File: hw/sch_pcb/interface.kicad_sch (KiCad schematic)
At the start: 19 parts, among them J6 HEADER_2x15, U12 SN74LVC2T45DCU, U13 SN74LVC2T45DCU, U14 SN74LVC2T45DCU, U6 AT24CS64-SSHM

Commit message: Update silkscreen and title blocks.
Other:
- title: AIRDOS04A base board -> USTSIPIN03A

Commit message: FIX USTIDs.
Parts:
- R11: UST_ID (none) -> 5c70984612875079b91f899f
- U12, U13, U14: UST_ID (none) -> 65555a850c8d609e3e79abde
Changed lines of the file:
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@@
+      (effects (font (size 1.27 1.27)) hide)
+    )
+    (property "UST_ID" "65555a850c8d609e3e79abde" (at 109.22 99.06 0)
       (effects (font (size 1.27 1.27)) hide)
     )
@@
       (effects (font (size 1.27 1.27)) hide)
     )
+    (property "UST_ID" "65555a850c8d609e3e79abde" (at 66.04 99.06 0)
+      (effects (font (size 1.27 1.27)) hide)
+    )
     (pin "1")
     (pin "2")
@@
       (effects (font (size 1.27 1.27)) hide)
     )
-    (property "UST_ID" "" (at 72.39 157.48 0)
+    (property "UST_ID" "5c70984612875079b91f899f" (at 72.39 157.48 0)
       (effects (font (size 1.27 1.27)) hide)
     )
@@
       (effects (font (size 1.27 1.27)) hide)
     )
-    (property "UST_ID" "" (at 77.47 157.48 0)
+    (property "UST_ID" "5c70984612875079b91f899f" (at 77.47 157.48 0)
       (effects (font (size 1.27 1.27)) hide)
     )
@@
       (effects (font (size 1.27 1.27)) hide)
     )
+    (property "UST_ID" "65555a850c8d609e3e79abde" (at 157.48 99.06 0)
+      (effects (font (size 1.27 1.27)) hide)
+    )

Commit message: Add notes to power consumption.
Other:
- note added: "+1 mA max"
- note added: "16 μA"
- note added: "POWER INPUT 5.5 mA"
- note removed: "POWER INPUT"
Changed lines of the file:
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@@
     (stroke (width 0) (type default))
   )
-  (text "POWER INPUT" (at 213.36 35.56 0)
+  (text "+1 mA max" (at 50.8 151.13 0)
     (effects (font (size 1.524 1.524)) (justify left bottom))
   )
+  (text "16 μA" (at 153.67 68.58 0)
+    (effects (font (size 1.27 1.27)) (justify left bottom))
+  )
+  (text "16 μA" (at 60.96 67.31 0)
+    (effects (font (size 1.524 1.524)) (justify left bottom))
+  )
+  (text "POWER INPUT 5.5 mA " (at 207.01 34.29 0)
+    (effects (font (size 1.524 1.524)) (justify left bottom))
+  )
+  (text "16 μA" (at 105.41 67.31 0)
+    (effects (font (size 1.27 1.27)) (justify left bottom))
+  )
   (label "3v3" (at 106.68 73.66 90) (fields_autoplaced)

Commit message: Flip side of pinheader connector. Resolve #7
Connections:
- net A0: now also J6.9; no longer J6.10
- net A1: now also J6.11; no longer J6.12
- net B0: now also J6.15; no longer J6.16
- net B1: now also J6.13; no longer J6.14
- net C0: now also J6.19; no longer J6.20
- net C1: now also J6.17; no longer J6.18
- net RX: now also J6.12; no longer J6.11
- net SOCKET_MISO: now also J6.18; no longer J6.17
- net SOCKET_MOSI: now also J6.16; no longer J6.15
- net SOCKET_SCLK: now also J6.20; no longer J6.19
- net TX: now also J6.14; no longer J6.13
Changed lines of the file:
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@@
     )
   )
-  (symbol (lib_id "MLAB_HEADER:HEADER_2x15") (at 246.38 68.58 90) (unit 1)
+  (symbol (lib_id "MLAB_HEADER:HEADER_2x15") (at 246.38 68.58 90) (mirror x) (unit 1)
     (in_bom yes) (on_board yes) (dnp no)
-    (property "Reference" "J6" (at 226.06 67.31 90)
+    (property "Reference" "J6" (at 226.06 69.85 90)
       (effects (font (size 1.524 1.524)) (justify left))
     )

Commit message: Swap MISO and MOSI traces. Resolve #4
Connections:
- net MISO: now also U14.6 (2B); no longer U12.7 (1B)
- net MOSI: now also U12.7 (1B); no longer U14.6 (2B)
- net SOCKET_MISO: now also U14.3 (2A); no longer U12.2 (1A)
- net SOCKET_MOSI: now also U12.2 (1A); no longer U14.3 (2A)
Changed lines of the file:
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@@
     (effects (font (size 1.27 1.27)) (justify right bottom))
   )
-  (label "SOCKET_MOSI" (at 146.05 101.6 180) (fields_autoplaced)
+  (label "SOCKET_MOSI" (at 54.61 96.52 180) (fields_autoplaced)
     (effects (font (size 1.524 1.524)) (justify right bottom))
   )
@@
     (effects (font (size 1.27 1.27)) (justify right bottom))
   )
-  (label "SOCKET_MISO" (at 54.61 96.52 180) (fields_autoplaced)
+  (label "SOCKET_MISO" (at 146.05 101.6 180) (fields_autoplaced)
     (effects (font (size 1.524 1.524)) (justify right bottom))
   )
@@
     (effects (font (size 1.524 1.524)) (justify left))
   )
-  (hierarchical_label "MISO" (shape input) (at 77.47 96.52 0) (fields_autoplaced)
+  (hierarchical_label "MISO" (shape input) (at 170.18 101.6 0) (fields_autoplaced)
     (effects (font (size 1.524 1.524)) (justify left))
   )
-  (hierarchical_label "MOSI" (shape output) (at 170.18 101.6 0) (fields_autoplaced)
+  (hierarchical_label "MOSI" (shape output) (at 77.47 96.52 0) (fields_autoplaced)
     (effects (font (size 1.524 1.524)) (justify left))
   )

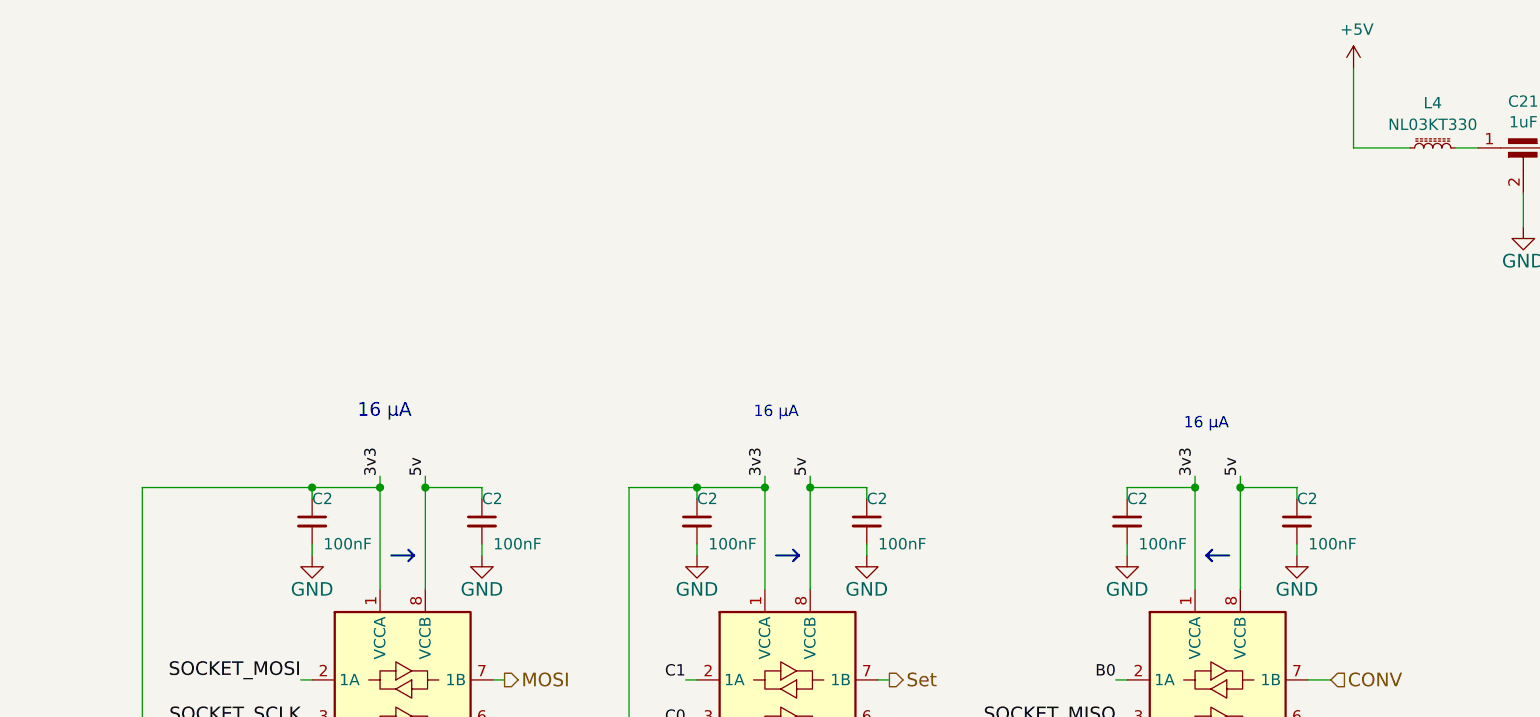
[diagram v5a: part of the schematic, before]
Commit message: Add LDO to power 3.3V translators. Resolve #3
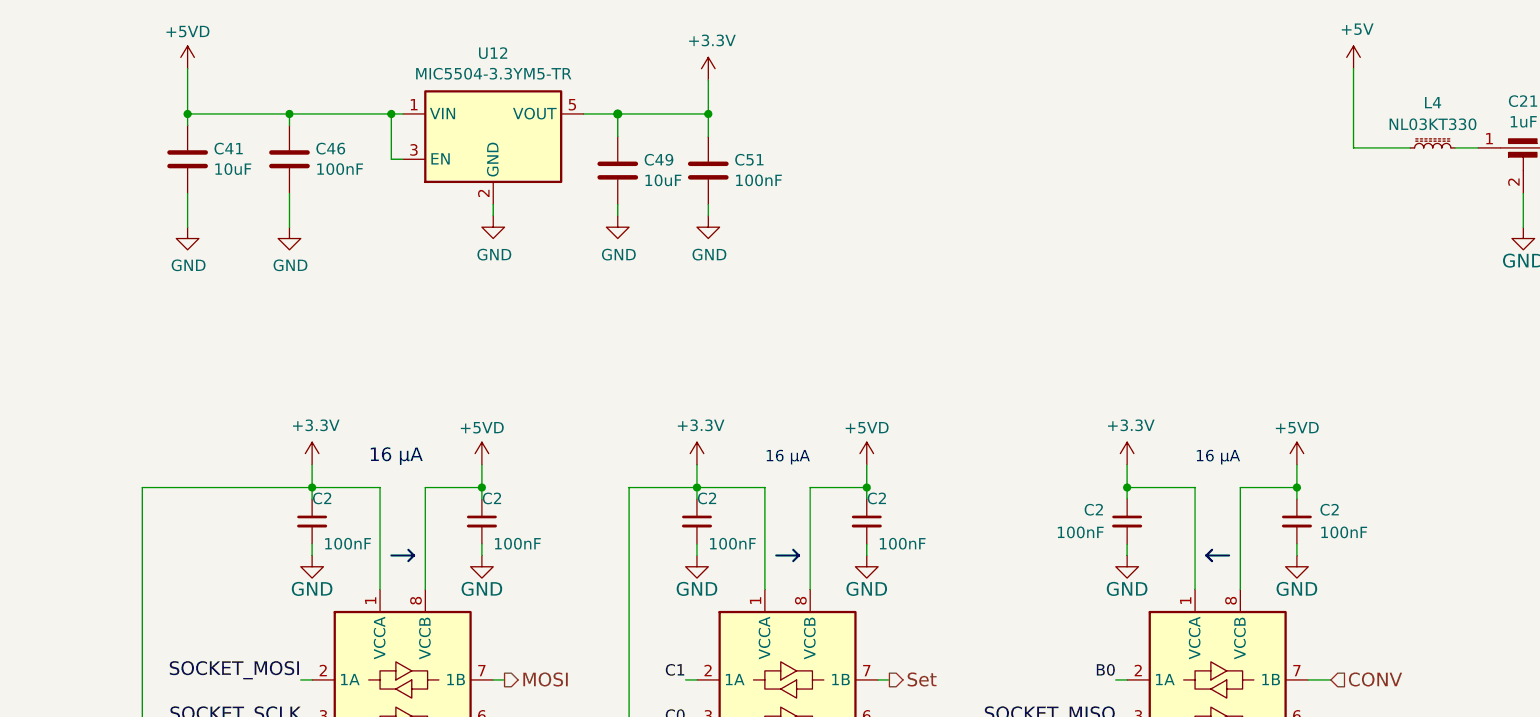
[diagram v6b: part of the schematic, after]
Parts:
- added C41, C49: 10uF, Capacitor_SMD:C_0805_2012Metric, symbol Device:C
- added C46, C51: 100nF, Capacitor_SMD:C_0805_2012Metric, symbol Device:C
- added U12: MIC5504-3.3YM5-TR, Package_TO_SOT_SMD:SOT-23-5, symbol Regulator_Linear:MIC5504-3.3YM5
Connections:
- net +5VD: now also C41.1, C46.1, U12.1 (VIN), U12.3 (EN)
- net 3v3: no longer C2.1, C2.1, C2.1, U12.1 (VCCA), U12.5 (DIR), U13.1 (VCCA), U13.5 (DIR), U14.1 (VCCA)
- net GND: now also C41.2, C46.2, C49.2, C51.2, U12.2 (GND)
- new net +3.3V: C2.1, C2.1, C2.1, C49.1, C51.1, U12.1 (VCCA), U12.5 (DIR), U12.5 (VOUT), U13.1 (VCCA), U13.5 (DIR), U14.1 (VCCA)

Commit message: Uniform capacitor types.
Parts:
- C1, C4: UST_ID 5c70984812875079b91f8bbe -> 5c70984712875079b91f8b53
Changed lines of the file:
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@@
       (effects (font (size 1.27 1.27)) hide)
     )
-    (property "UST_ID" "5c70984812875079b91f8bbe" (at 213.36 41.91 0)
+    (property "UST_ID" "5c70984712875079b91f8b53" (at 213.36 41.91 0)
       (effects (font (size 1.27 1.27)) hide)
     )
@@
       (effects (font (size 1.27 1.27)) hide)
     )
-    (property "UST_id" "" (at 22.86 165.1 0)
-      (effects (font (size 1.27 1.27)) hide)
-    )
-    (property "UST_ID" "5c70984812875079b91f8bbe" (at -219.71 194.31 0)
-      (effects (font (size 1.27 1.27)) hide)
-    )
+    (property "UST_ID" "5c70984712875079b91f8b53" (at -219.71 194.31 0)
+      (effects (font (size 1.27 1.27)) hide)
+    )

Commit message: Update Kicad project version.
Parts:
- renumbered C21 to C37, C4 to C39
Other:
- company: Jakub Kákona <info@ust.cz> -> kaklik <info@ust.cz>
- title: USTSIPIN03A -> USTSIPIN03B
